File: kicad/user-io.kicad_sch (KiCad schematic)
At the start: 46 parts, among them J1 USB1, J2 Lower Bank, J3 Upper Bank, SW1 PTS815, U1 MIMXRT1171DVMAB, U2 MAYA-W166-00B, U3 LSM6DSV, U4 LIS2MDL, U5 RTMC-G2-4IQ48, Y1 8MHz

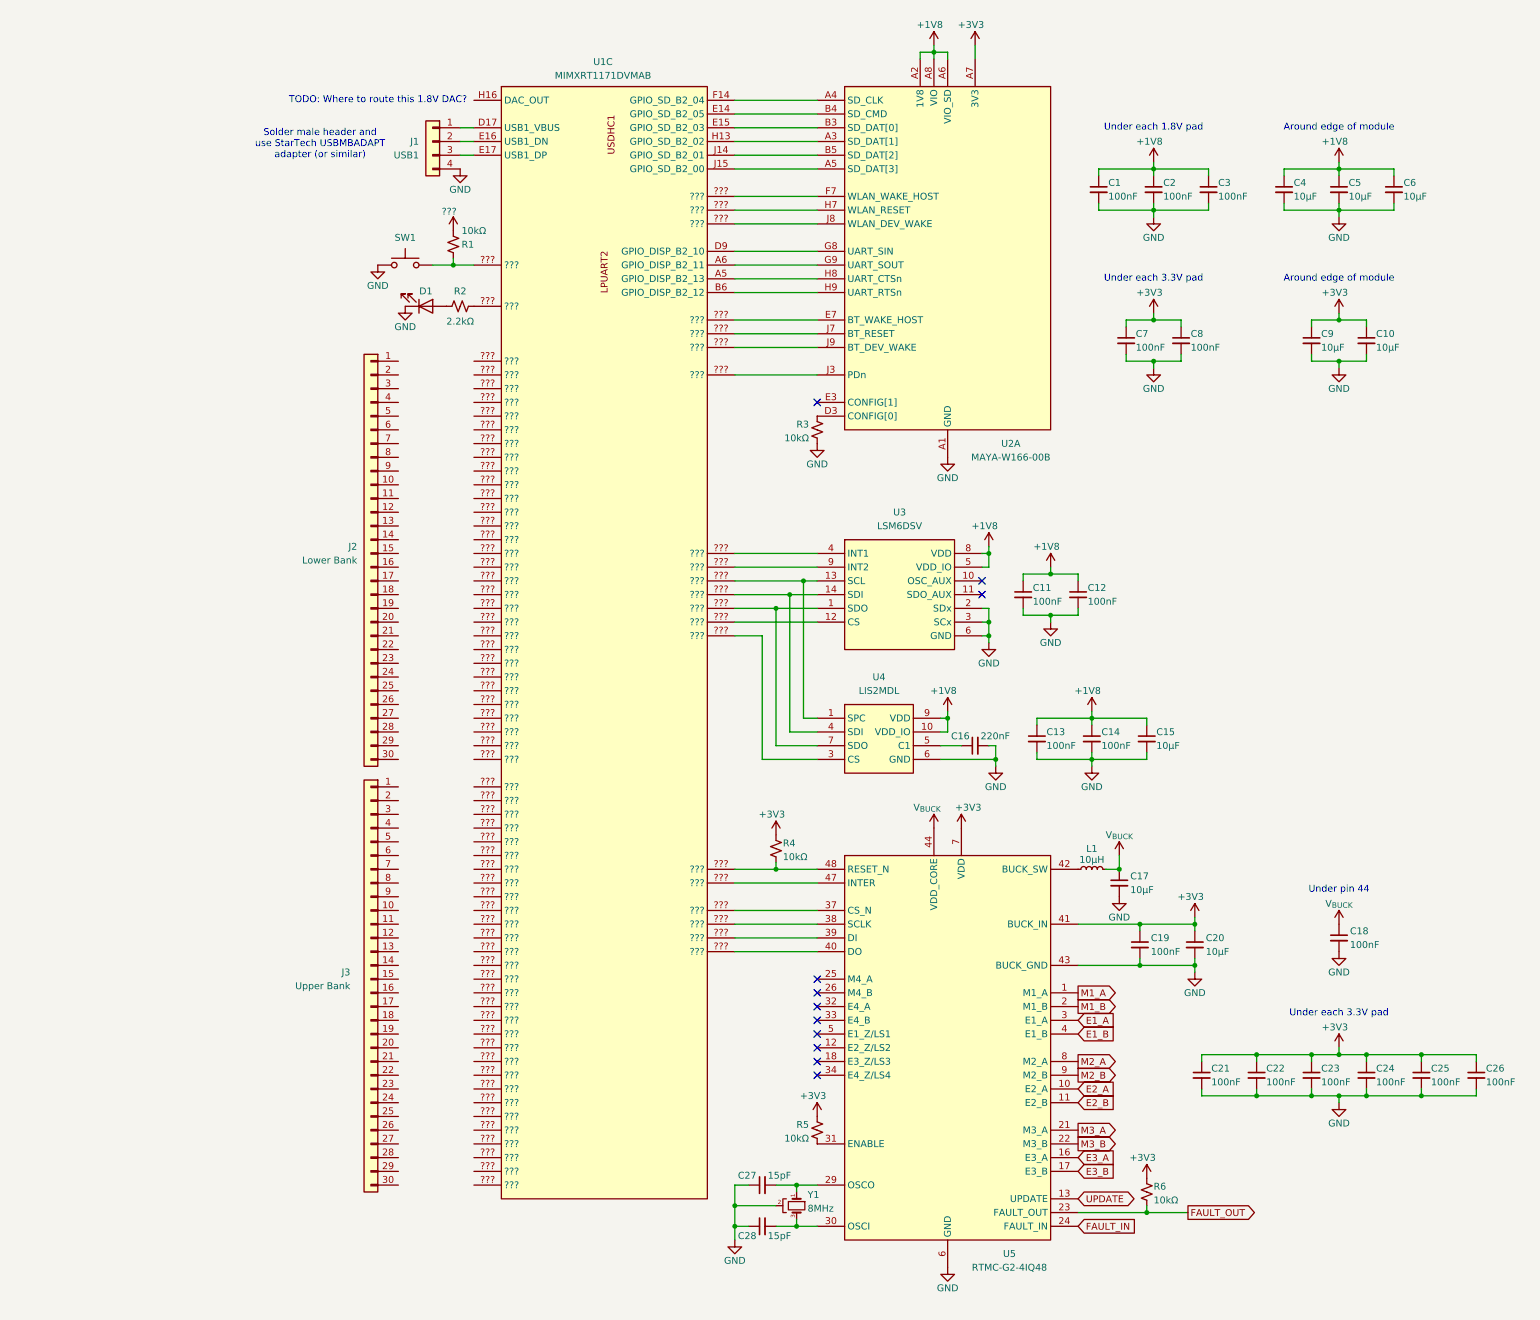
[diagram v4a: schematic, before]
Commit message: reworked bypass capacitors for MIMXRT1171DVMAB
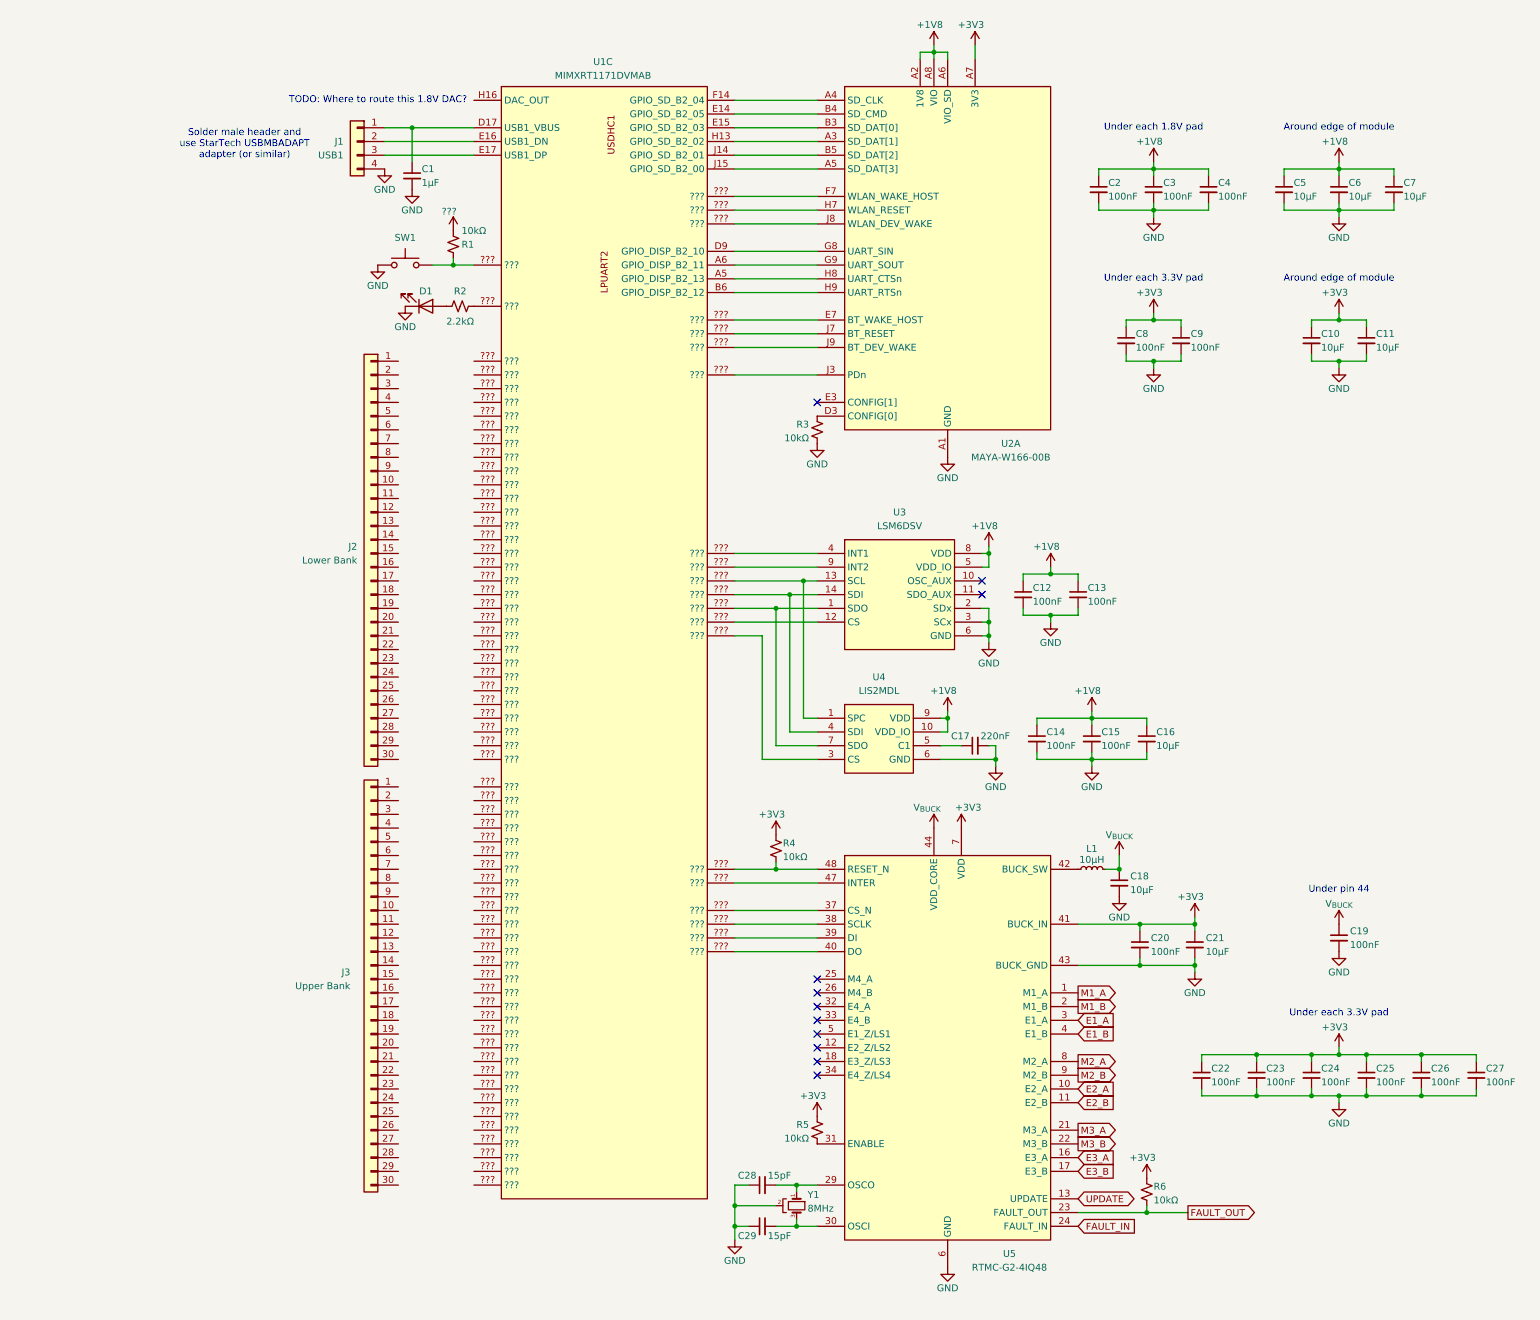
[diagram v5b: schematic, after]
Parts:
- added C1: 1μF, symbol Device:C_Small
- renumbered C9 to C10, C10 to C11, C11 to C12, C12 to C13, C13 to C14, C14 to C15, C15 to C16, C16 to C17, C17 to C18, C18 to C19, C1 to C2, C19 to C20, C20 to C21, C21 to C22, C22 to C23, C23 to C24, C24 to C25, C25 to C26, C26 to C27, C27 to C28, C28 to C29, C2 to C3, C3 to C4, C4 to C5, C5 to C6, C6 to C7, C7 to C8, C8 to C9
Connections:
- net GND: now also C1.2
- net at J1.1 (Pin_1), U1.D17 (USB1_VBUS): now also C1.1
- net at U1.???: now also U2.J9 (BT_DEV_WAKE)
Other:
- moved on the sheet: J1

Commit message: reworked USB circuitry
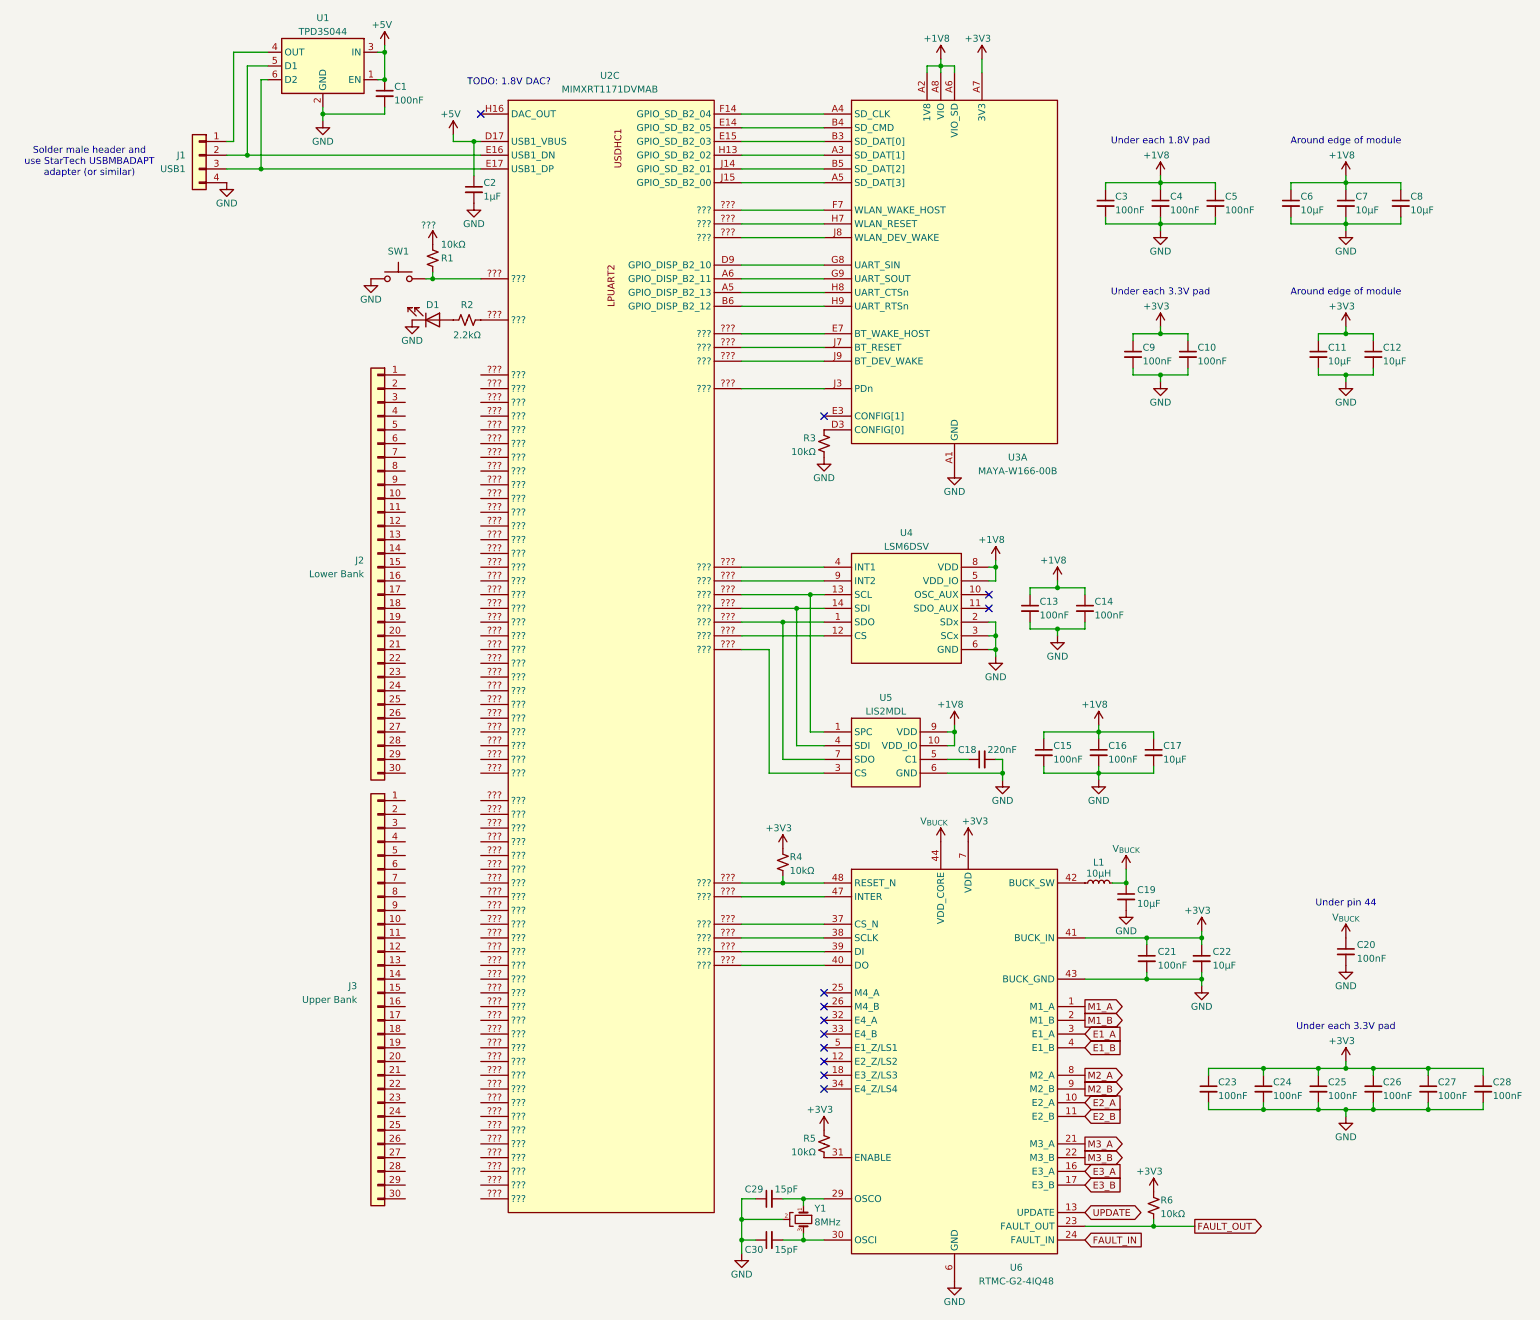
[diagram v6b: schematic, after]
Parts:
- added C1: 100nF, symbol Device:C_Small
- added U1: TPD3S044, Package_TO_SOT_SMD:SOT-23-6, symbol Power_Protection:TPD3S044
- renumbered C9 to C10, C10 to C11, C11 to C12, C12 to C13, C13 to C14, C14 to C15, C15 to C16, C16 to C17, C17 to C18, C18 to C19, C1 to C2, C19 to C20, C20 to C21, C21 to C22, C22 to C23, C23 to C24, C24 to C25, C25 to C26, C26 to C27, C27 to C28, C28 to C29, C2 to C3, C29 to C30, C3 to C4, C4 to C5, C5 to C6, C6 to C7, C7 to C8, C8 to C9, U1 to U2, U2 to U3, U3 to U4, U4 to U5, U5 to U6
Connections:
- net GND: now also C1.2, U1.2 (GND)
- net +5V: now reaches C2.1, U2.D17 (USB1_VBUS)
- net +5V: now also C1.1, U1.1 (EN), U1.3 (IN); no longer J1.1 (Pin_1)
- net at J1.2 (Pin_2), U2.E16 (USB1_DN): now also U1.5 (D1)
- net at J1.3 (Pin_3), U2.E17 (USB1_DP): now also U1.6 (D2)
- net at U2.???: now also U3.J9 (BT_DEV_WAKE)
- new net: J1.1 (Pin_1), U1.4 (OUT)
- no-connect marks 11 -> 12
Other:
- note added: "TODO: 1.8V DAC?"
- note removed: "TODO: Where to route this 1.8V DAC?"
- moved on the sheet: C10, C11, C12, C13, C14, C15, C16, C17, C18, C19, C2, C20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

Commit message: added remaining footprints
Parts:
- C1, C18, C2: footprint (none) -> Capacitor_SMD:C_0201_0603Metric
- U1: footprint Package_TO_SOT_SMD:SOT-23-6 -> project_footprints:TPD3S044
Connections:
- net at U2.???: now also U3.J9 (BT_DEV_WAKE)
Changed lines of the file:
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@@
 			)
 		)
-		(property "Footprint" "Package_TO_SOT_SMD:SOT-23-6"
+		(property "Footprint" "project_footprints:TPD3S044"
 			(at 81.28 16.51 0)
 			(hide yes)
@@
 			)
 		)
-		(property "Footprint" ""
+		(property "Footprint" "Capacitor_SMD:C_0201_0603Metric"
 			(at 109.22 48.26 0)
 			(hide yes)
@@
 			)
 		)
-		(property "Footprint" ""
+		(property "Footprint" "Capacitor_SMD:C_0201_0603Metric"
 			(at 92.71 30.48 0)
 			(hide yes)
@@
 			)
 		)
-		(property "Footprint" ""
+		(property "Footprint" "Capacitor_SMD:C_0201_0603Metric"
 			(at 203.2 153.67 0)
 			(hide yes)

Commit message: removed USB host and 1.8V DAC
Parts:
- removed C1: 100nF, Capacitor_SMD:C_0201_0603Metric, symbol Device:C_Small
- removed C2: 1μF, Capacitor_SMD:C_0201_0603Metric, symbol Device:C_Small
- removed J1: USB1, project_footprints:Header-1x04, symbol Connector_Generic:Conn_01x04
- removed J3: Upper Bank, project_footprints:Header-1x30, symbol Connector_Generic:Conn_01x30
- removed U1: TPD3S044, project_footprints:TPD3S044, symbol Power_Protection:TPD3S044
- added J1: Lower Bank, project_footprints:Header-1x30, symbol Connector_Generic:Conn_01x30
- J2: value Lower Bank -> Upper Bank
- U1: renamed from U2; footprint project_footprints:MIMXRT1171DVMAB -> Package_BGA:MAPBGA-289_14x14mm_Layout17x17_P0.8mm
- renumbered C3 to C1, C12 to C10, C13 to C11, C14 to C12, C15 to C13, C16 to C14, C17 to C15, C18 to C16, C19 to C17, C20 to C18, C21 to C19, C4 to C2, C22 to C20, C23 to C21, C24 to C22, C25 to C23, C26 to C24, C27 to C25, C28 to C26, C29 to C27, C30 to C28, C5 to C3, C6 to C4, C7 to C5, C8 to C6, C9 to C7, C10 to C8, C11 to C9, U3 to U2, U4 to U3, U5 to U4, U6 to U5
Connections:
- net at U1.???: now also U2.J9 (BT_DEV_WAKE)
- removed net +5V: U1.D17 (USB1_VBUS)
- no-connect marks 12 -> 11
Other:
- note removed: "Solder male header and use StarTech USBMBADAPT adapter (or similar)"
- note removed: "TODO: 1.8V DAC?"
